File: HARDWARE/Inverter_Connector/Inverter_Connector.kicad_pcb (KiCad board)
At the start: 2 copper layers, 58.4 x 20 mm, 7 parts, among them J1 M300-MV30645M1, J2 1803277, J3 1803277, J4 1894820, J5 1881451, J6 1881451, J7 1881448

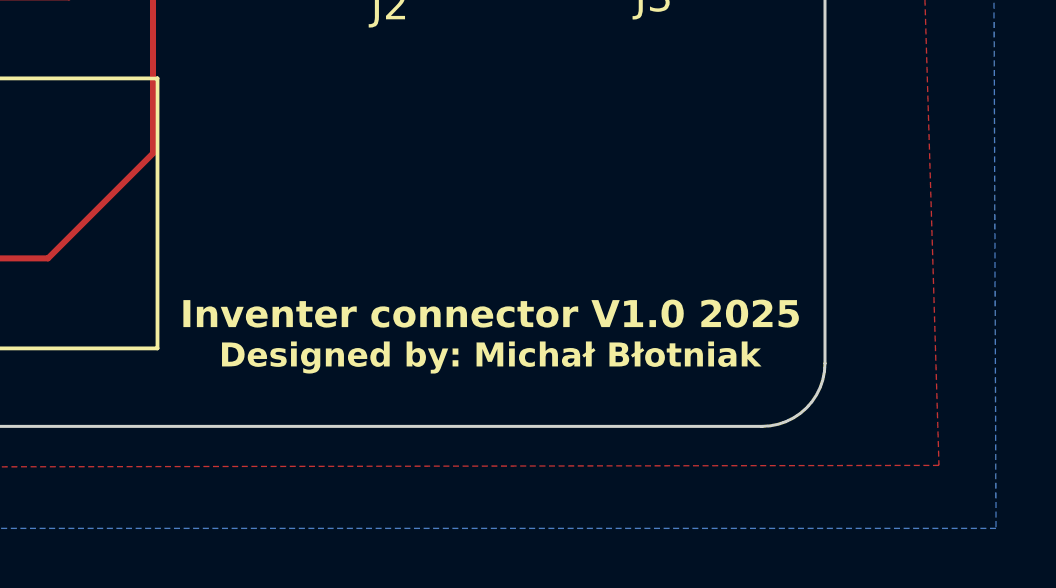
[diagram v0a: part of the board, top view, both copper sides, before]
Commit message: Corrected a typo
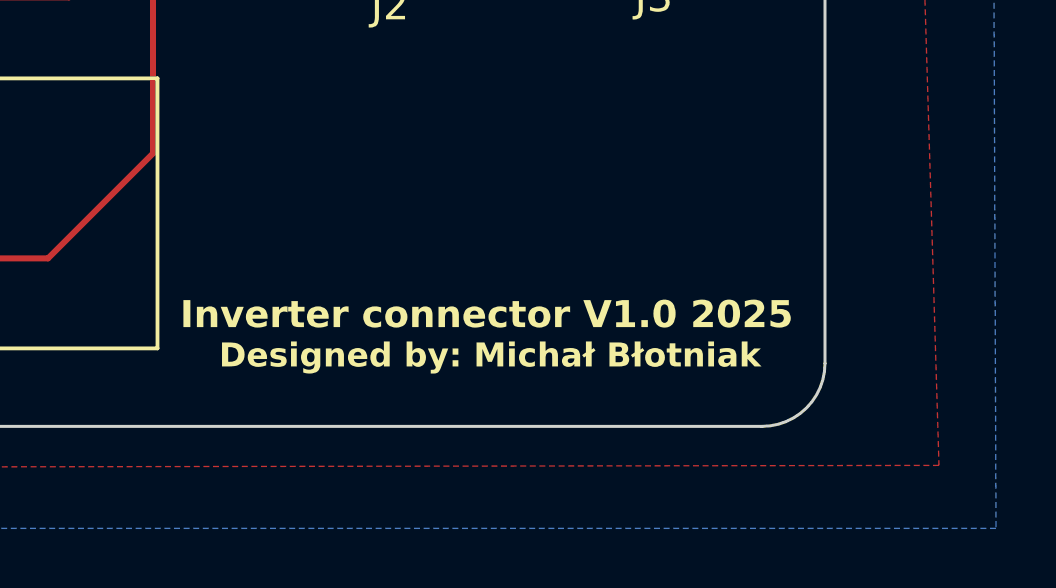
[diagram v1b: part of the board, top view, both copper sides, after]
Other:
- board text added: "Inverter connector V1.0 2025"
- board text removed: "Inventer connector V1.0 2025"
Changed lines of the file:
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@@
 		(layer "Edge.Cuts")
 	)
-	(gr_text "Inventer connector V1.0 2025"
+	(gr_text "Inverter connector V1.0 2025"
 		(at 153.7 105.2 0)
 		(layer "F.SilkS" knockout)

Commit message: Version 1.0
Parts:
- moved J2 1.96 mm to (159.1, 90.6)
- moved J3 1.89 mm to (167.9, 90.6)
- moved J7 0.20 mm to (153.0, 91.5)
- moved J5 0.15 mm to (141.2, 91.5)
- moved J4 0.06 mm to (120.1, 91.6)
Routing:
- net VCC: track 9.27 -> 11.9 mm
- net GND: track 5.74 -> 7.55 mm

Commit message: After fix Version 1.1
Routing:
- net TEMP_P: track 17.1 -> 30.0 mm
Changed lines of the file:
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@@
 	)
 	(segment
-		(start 150.55 91.75)
-		(end 150.3 91.5)
-		(width 0.2)
-		(layer "F.Cu")
-		(net 5)
-	)
-	(segment
-		(start 150.55 93.55)
-		(end 150.55 91.75)
-		(width 0.2)
-		(layer "F.Cu")
-		(net 5)
-	)
-	(segment
-		(start 143.8 96.4)
-		(end 146.1 94.1)
-		(width 0.2)
-		(layer "F.Cu")
-		(net 5)
-	)
-	(segment
-		(start 146.1 94.1)
-		(end 150 94.1)
-		(width 0.2)
-		(layer "F.Cu")
-		(net 5)
-	)
-	(segment
-		(start 143.8 101.3)
-		(end 143.8 96.4)
+		(start 143.8 104.3)
+		(end 149.4 104.3)
 		(width 0.2)
 		(layer "F.Cu")
@@
 	(segment
 		(start 142.3 102.8)
-		(end 143.8 101.3)
+		(end 143.8 104.3)
 		(width 0.2)
 		(layer "F.Cu")
@@
 	)
 	(segment
-		(start 150 94.1)
-		(end 150.55 93.55)
+		(start 151.8 89.6)
+		(end 150.49 90.91)
 		(width 0.2)
 		(layer "F.Cu")
+		(net 5)
+	)
+	(segment
+		(start 150.49 90.91)
+		(end 150.49 91.5454)
+		(width 0.2)
+		(layer "F.Cu")
+		(net 5)
+	)
+	(segment
+		(start 154.4 89.6)
+		(end 151.8 89.6)
+		(width 0.2)
+		(layer "F.Cu")
+		(net 5)
+	)
+	(segment
+		(start 149.4 104.3)
+		(end 154.9 98.8)
+		(width 0.2)
+		(layer "F.Cu")
+		(net 5)
+	)
+	(segment
+		(start 154.9 98.8)
+		(end 154.9 90.1)
+		(width 0.2)
+		(layer "F.Cu")
+		(net 5)
+	)
+	(segment
+		(start 154.9 90.1)
+		(end 154.4 89.6)
+		(width 0.2)
+		(layer "F.Cu")
